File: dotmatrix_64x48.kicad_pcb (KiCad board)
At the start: 2 copper layers, 226 x 136 mm, 882 parts, among them J1 CONN_01X04, J2 CONN_01X05, P3 CONN_01X06, P6 CONN_01X03, Q1 Q_NPN_BCE RN5006, Q10 AO3401, Q11 AO3401, Q12 AO3401, Q13 AO3401, Q14 AO3401, Q15 AO3401, Q16 AO3401, Q17 AO3401, Q18 AO3401, Q19 AO3401, Q2 Q_NPN_BEC, Q20 AO3401, Q21 AO3401, Q22 AO3401, Q23 AO3401, Q24 AO3401, Q25 AO3401, Q26 AO3401, Q27 AO3401, Q28 AO3401, Q29 AO3401, Q3 NJL7302L-F3, Q30 Q_NPN_BEC, Q4 Q_NPN_BEC, Q5 AO3401, Q6 AO3401, Q7 AO3401, Q8 AO3401, Q9 AO3401, SW1 SW_PUSH_SMALL_H, SW2 SW_PUSH_SMALL_H, SW3 SW_PUSH_SMALL_H, SW4 SW_PUSH_SMALL_H, SW5 SW_PUSH_SMALL_H, SW6 SW_PUSH_SMALL_H, SW7 SW_PUSH_SMALL_H, SW8 SW_PUSH_SMALL_H, T1 COMMON_MODE_CHOKE, U1 WROOM-02, U10 LED1642GW, U11 74HCT595, U12 AE-BME280, U13 74HCT595, U14 NJM2845DL1-33, U15 74HCT595, U17 OSRB38C9AA, U18 BME280, U19 PIC32MX220F032B-I/ML, U2 74VHC541, U3 LED1642GW, U4 LED1642GW, U5 LED1642GW, U6 LED1642GW, U7 LED1642GW, U8 LED1642GW, U9 LED1642GW, Y1 8MHz

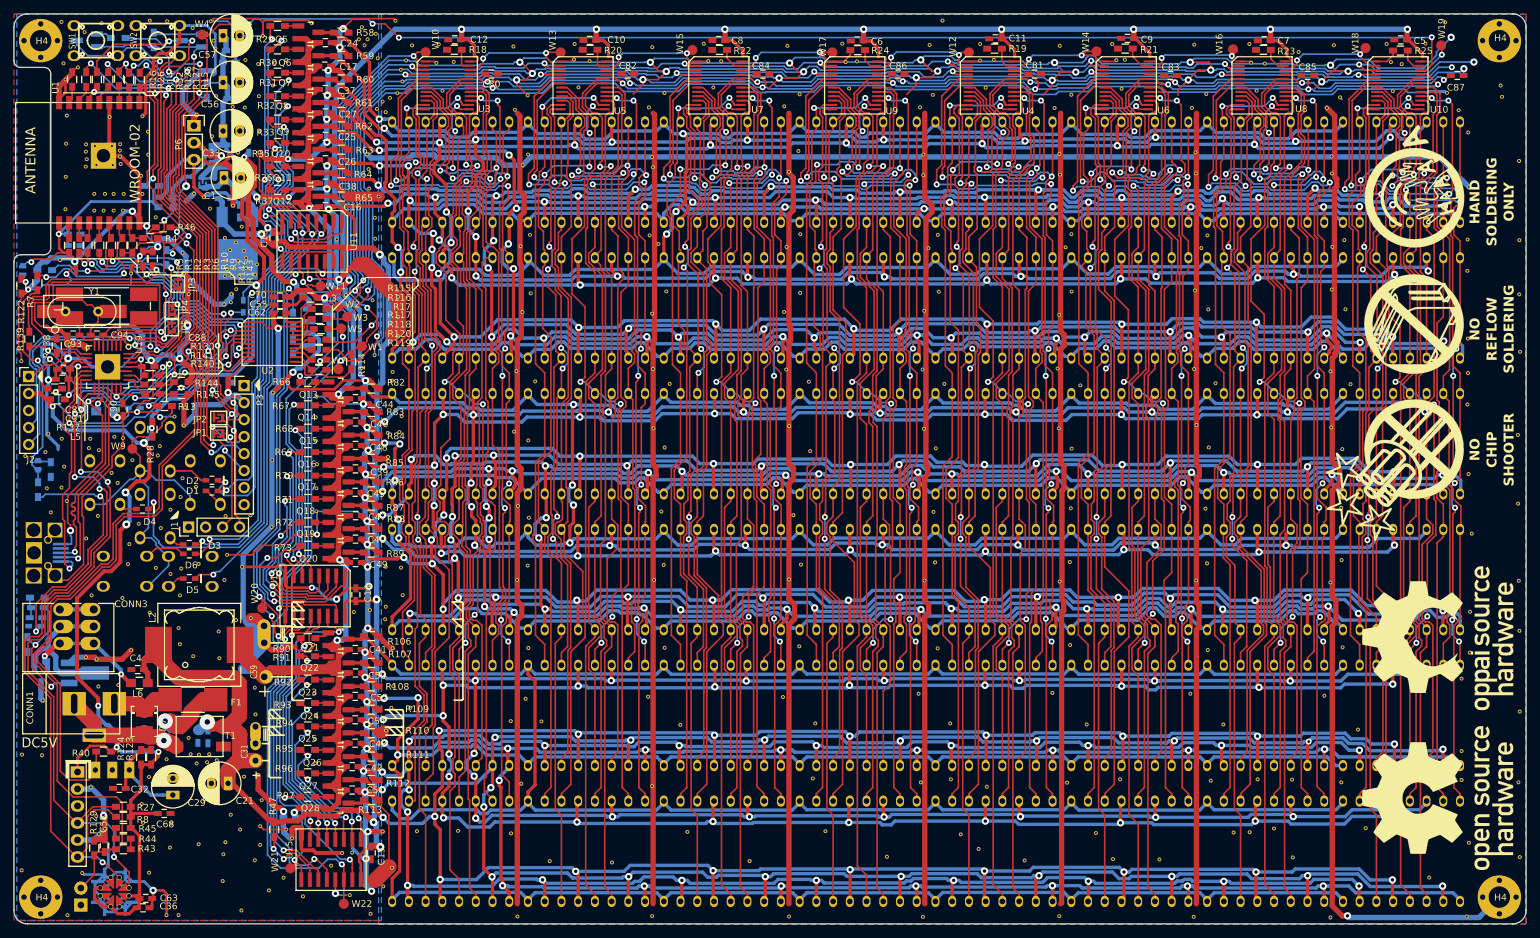
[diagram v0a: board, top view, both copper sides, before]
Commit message: DRC clear; This project likely to be abandoned due to 4MiB Flash version WROOM-02 shortage.
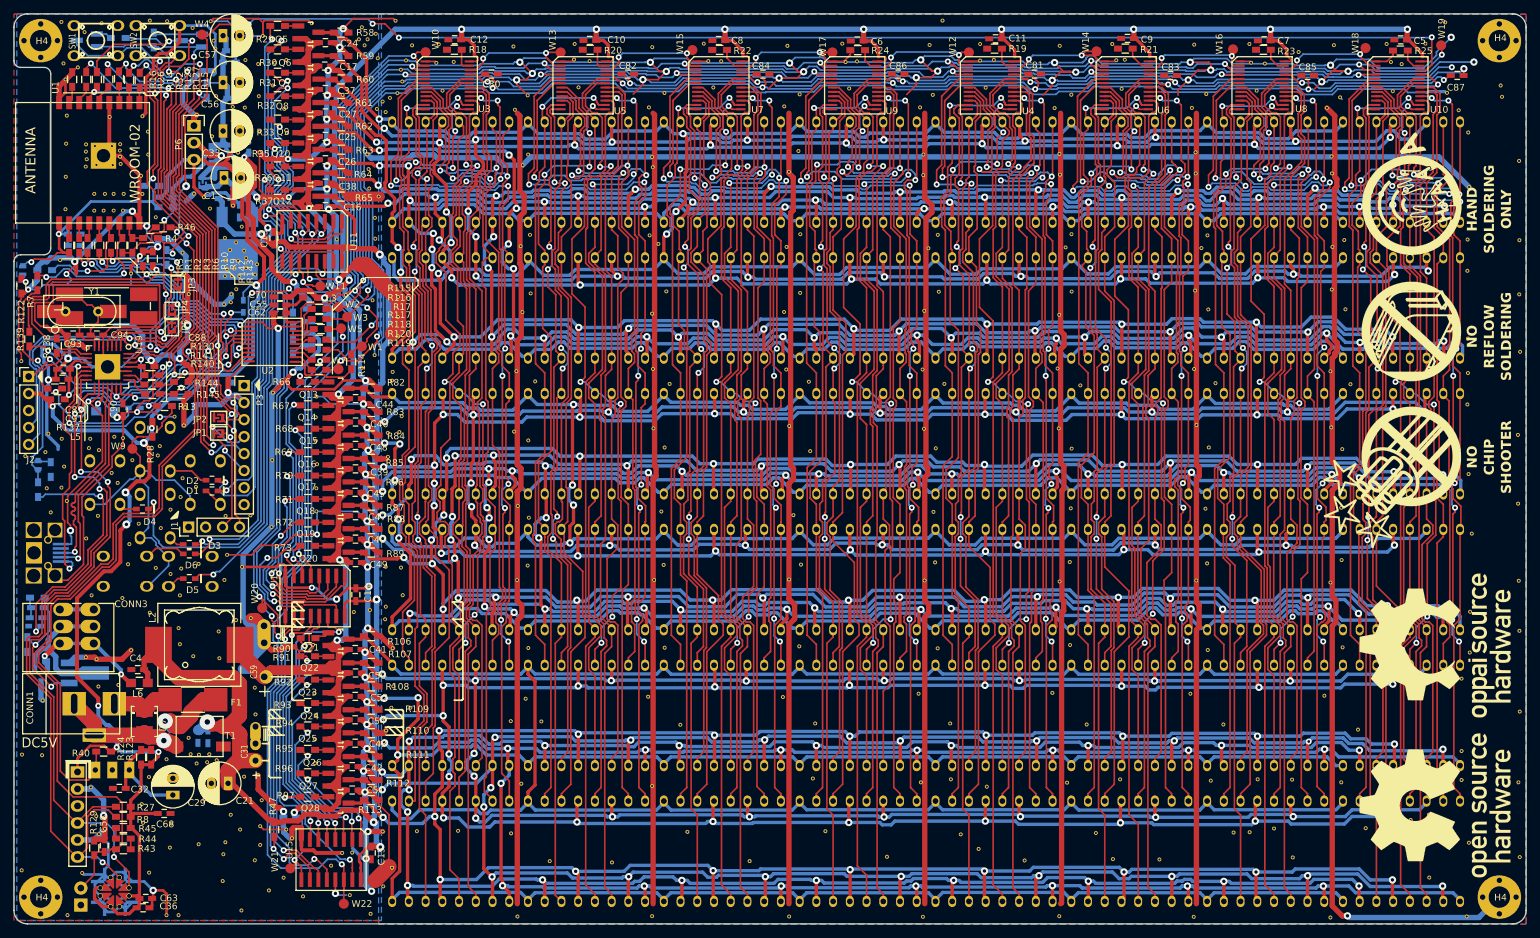
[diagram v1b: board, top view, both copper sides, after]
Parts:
- added REF**: stitch-via-0.6mm, components:stitch-via-0.6mm, F.Cu at (52.8, 29.8)
- added REF**: stitch-via-0.6mm, components:stitch-via-0.6mm, F.Cu at (52.4, 26.2)
- moved G*** 1.17 mm to (222.0, 85.3)
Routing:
- net GND: track 3088.4 -> 3084.8 mm
- net /row_driver/SEL4: track 100.5 -> 103.5 mm
- net /row_driver/SEL5: track 86.1 -> 85.6 mm

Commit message: This is the MazoClock hw 4.0 series; Uses ESP32 processor instead of ESP8266 used in prior MazoClock hw 3.0 series.
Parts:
- removed C33, C56, C57: 100u, components:C_Radial_D6.3_L11.2_P2.5_hand_soldering
- removed C34, C35, C69, C71: 1u, Capacitors_SMD:C_0603_HandSoldering
- removed C61: 0.1u, Capacitors_SMD:C_0603_HandSoldering
- removed D10, D8: Led_Small, components:LED1608_Handsoldering
- removed JP13: Jumper_NC_Small, components:SolderJumper
- removed L1: BLM21PG331SN 300R@100MHz, Capacitors_SMD:C_0805_HandSoldering
- removed L4, L7: BLM18RK102SN1 1k @ 100MHz, Resistors_SMD:R_0603_HandSoldering
- removed P3: CONN_01X06, Pin_Headers:Pin_Header_Straight_1x08_Pitch2.54mm
- removed P6: CONN_01X03, Pin_Headers:Pin_Header_Straight_1x03
- removed R121, R142, R143, R144, R145, R38, R39: 22k, Resistors_SMD:R_0603_HandSoldering
- removed R122: 4.7k, Resistors_SMD:R_0603_HandSoldering
- removed R126, R127, R46, R52: 120R, Resistors_SMD:R_0603_HandSoldering
- removed R48: 1k, Resistors_SMD:R_0603_HandSoldering
- removed R54, R55: 10k, Resistors_SMD:R_0603_HandSoldering
- removed the REF** at (48.5, 19.5)
- removed the REF** at (45.5, 48.9)
- removed the REF** at (18.9, 48.8)
- removed the REF** at (229.9, 89.7)
- removed the REF** at (38.9, 38.9)
- removed the REF** at (210.4, 93.6)
- removed the REF** at (229.4, 80.8)
- removed the REF** at (229.2, 70.4)
- removed the REF** at (229.3, 65.7)
- removed the REF** at (44.4, 55.1)
- removed the REF** at (211.8, 67.3)
- removed the REF** at (45.2, 53.1)
- removed the REF** at (46.4, 47.4)
- removed the REF** at (44.3, 47.3)
- removed the REF** at (46.0, 43.8)
- removed the REF** at (44.8, 40.6)
- removed the REF** at (229.3, 60.5)
- removed the REF** at (43.5, 45.5)
- removed the REF** at (45.2, 46.1)
- removed the REF** at (65.6, 54.8)
- removed the REF** at (65.1, 38.1)
- removed the REF** at (65.0, 35.2)
- removed the REF** at (64.8, 33.0)
- removed the REF** at (41.9, 16.0)
- removed the REF** at (47.1, 31.2)
- removed the REF** at (31.0, 36.2)
- removed the REF** at (32.0, 29.6)
- removed the REF** at (19.8, 36.4)
- removed the REF** at (19.8, 31.4)
- removed the REF** at (21.6, 20.0)
- removed the REF** at (46.5, 26.0)
- removed the REF** at (24.3, 131.9)
- removed the REF** at (13.2, 140.0)
- removed the REF** at (46.6, 18.9)
- removed the REF** at (66.0, 45.6)
- removed the REF** at (42.2, 24.3)
- removed the REF** at (50.6, 78.7)
- removed the REF** at (38.1, 120.2)
- removed the REF** at (45.2, 102.6)
- removed the REF** at (36.8, 106.2)
- removed the REF** at (44.7, 25.9)
- removed the REF** at (35.5, 133.0)
- removed the REF** at (38.8, 108.0)
- removed the REF** at (42.6, 104.3)
- removed the REF** at (32.3, 101.5)
- removed the REF** at (36.6, 103.8)
- removed the REF** at (35.3, 136.6)
- removed the REF** at (44.4, 131.7)
- removed the REF** at (46.4, 126.0)
- removed the REF** at (43.3, 137.6)
- removed the REF** at (45.8, 133.9)
- removed the REF** at (43.6, 135.8)
- removed the REF** at (39.6, 136.1)
- removed the REF** at (32.1, 33.0)
- removed the REF** at (38.1, 53.9)
- removed the REF** at (22.7, 34.8)
- removed the REF** at (22.9, 33.7)
- removed the REF** at (22.8, 32.6)
- removed the REF** at (22.8, 31.5)
- removed the REF** at (26.6, 31.8)
- removed the REF** at (24.1, 31.8)
- removed the REF** at (24.3, 34.6)
- removed the REF** at (26.8, 34.6)
- removed the REF** at (27.9, 34.4)
- removed the REF** at (27.9, 33.4)
- removed the REF** at (27.8, 32.4)
- removed the REF** at (27.9, 31.5)
- removed the REF** at (22.6, 14.7)
- removed the REF** at (43.6, 87.0)
- removed the REF** at (34.8, 123.4)
- removed the REF** at (32.2, 126.0)
- removed the REF** at (39.3, 124.0)
- removed the REF** at (40.9, 123.8)
- removed the REF** at (42.3, 123.5)
- removed the REF** at (39.6, 122.7)
- removed the REF** at (38.4, 122.7)
- removed the REF** at (41.2, 122.7)
- removed the REF** at (40.5, 129.4)
- removed the REF** at (42.7, 108.3)
- removed the REF** at (66.0, 42.5)
- removed the REF** at (45.5, 32.7)
- removed the REF** at (61.1, 24.1)
- removed the REF** at (66.4, 18.6)
- removed the REF** at (30.6, 88.2)
- removed the REF** at (46.1, 94.7)
- removed the REF** at (43.5, 96.6)
- removed the REF** at (34.0, 88.8)
- removed the REF** at (29.2, 91.2)
- removed the REF** at (47.4, 87.0)
- removed the REF** at (22.8, 108.2)
- removed the REF** at (44.6, 51.2)
- removed the REF** at (46.7, 50.0)
- removed the REF** at (45.0, 50.1)
- removed the REF** at (43.8, 50.1)
- removed the REF** at (37.6, 70.8)
- removed the REF** at (36.0, 72.2)
- removed the REF** at (33.8, 76.6)
- removed the REF** at (23.2, 76.9)
- removed the REF** at (19.9, 84.8)
- removed the REF** at (48.0, 51.0)
- removed the REF** at (17.5, 86.5)
- removed the REF** at (19.1, 82.8)
- removed the REF** at (16.9, 82.9)
- removed the REF** at (13.7, 78.1)
- removed the REF** at (17.1, 74.8)
- removed the REF** at (39.2, 82.7)
- removed the REF** at (29.5, 50.8)
- removed the REF** at (19.7, 21.8)
- removed the REF** at (19.4, 19.4)
- removed the REF** at (41.6, 30.3)
- removed the REF** at (44.7, 20.7)
- removed the REF** at (44.7, 28.0)
- removed the REF** at (41.4, 13.1)
- removed the REF** at (34.9, 13.1)
- removed the REF** at (32.3, 13.0)
- removed the REF** at (35.4, 86.1)
- removed the REF** at (36.9, 84.2)
- removed the REF** at (27.5, 82.1)
- removed the REF** at (26.6, 80.6)
- removed the REF** at (33.2, 42.4)
- removed the REF** at (31.2, 38.9)
- removed the REF** at (26.3, 27.4)
- removed the REF** at (31.2, 27.3)
- removed the REF** at (19.9, 27.2)
- removed the REF** at (19.7, 41.2)
- removed the REF** at (19.1, 13.2)
- removed the REF** at (25.1, 13.4)
- removed the REF** at (38.7, 14.1)
- removed the REF** at (41.9, 20.5)
- removed the REF** at (29.1, 94.2)
- removed the REF** at (36.8, 98.9)
- removed the REF** at (43.9, 92.8)
- removed the REF** at (37.0, 94.9)
- removed the REF** at (35.4, 95.7)
- removed the REF** at (33.2, 94.8)
- removed the REF** at (39.6, 94.2)
- removed the REF** at (37.2, 81.4)
- removed the REF** at (33.5, 78.0)
- removed the REF** at (29.7, 78.7)
- removed the REF** at (28.4, 38.9)
- removed the REF** at (26.9, 38.9)
- removed the REF** at (25.6, 38.9)
- removed the REF** at (24.0, 38.9)
- removed the REF** at (28.3, 41.4)
- removed the REF** at (26.9, 41.4)
- removed the REF** at (25.4, 41.4)
- removed the REF** at (24.0, 41.4)
- removed the REF** at (37.2, 47.7)
- removed the REF** at (48.7, 29.6)
- removed the REF** at (48.7, 32.7)
- removed the REF** at (41.3, 41.1)
- removed the REF** at (40.4, 39.4)
- removed the REF** at (50.7, 68.6)
- removed the REF** at (37.4, 50.8)
- removed the REF** at (44.5, 53.9)
- removed the REF** at (43.5, 51.2)
- removed the REF** at (45.7, 51.2)
- removed the REF** at (46.7, 48.5)
- removed the REF** at (43.6, 48.9)
- removed the REF** at (43.4, 55.4)
- removed the REF** at (19.1, 75.5)
- removed the REF** at (28.3, 75.4)
- removed the REF** at (27.0, 75.2)
- removed the REF** at (23.4, 75.5)
- removed the REF** at (13.1, 63.9)
- removed the REF** at (37.4, 73.5)
- removed the REF** at (24.7, 77.2)
- removed the REF** at (19.5, 79.7)
- removed the REF** at (16.7, 77.5)
- removed the REF** at (22.8, 90.4)
- removed the REF** at (24.6, 87.0)
- removed the REF** at (28.2, 99.3)
- removed the REF** at (29.5, 107.1)
- removed the REF** at (24.7, 134.6)
- removed the REF** at (48.3, 49.4)
- removed the REF** at (46.0, 146.0)
- removed the REF** at (50.1, 143.0)
- removed the REF** at (43.2, 141.6)
- removed the REF** at (25.6, 133.8)
- removed the REF** at (31.3, 132.9)
- removed the REF** at (31.1, 130.1)
- removed the REF** at (23.5, 127.6)
- removed the REF** at (39.3, 27.1) (x2)
- removed the REF** at (42.1, 17.2)
- removed the REF** at (48.6, 24.3)
- removed SW1, SW2: SW_PUSH_SMALL_H, components:TACT-SW-4P
- removed W4, W5, W9: TEST_1P, Measurement_Points:Measurement_Point_Round-SMD-Pad_Small
- added C28: 1u, Capacitors_SMD:C_0603_HandSoldering, F.Cu at (28.9, 89.8)
- added C30: 1u, Capacitors_SMD:C_0603_HandSoldering, F.Cu at (30.3, 72.2)
- added J10: Conn_01x07_Female, Pin_Headers:Pin_Header_Straight_1x07_Pitch2.54mm, F.Cu at (254.4, 73.2)
- added J11: Conn_01x04_Female, Pin_Headers:Pin_Header_Straight_1x04_Pitch2.54mm, B.Cu at (50.2, 100.3)
- added J3: Conn_01x19_Female, Pin_Headers:Pin_Header_Straight_1x19_Pitch2.54mm, B.Cu at (26.2, 65.5)
- added J4: Conn_01x14_Female, Pin_Headers:Pin_Header_Straight_1x14_Pitch2.54mm, B.Cu at (14.5, 72.0)
- added J5: Conn_01x10_Female, Pin_Headers:Pin_Header_Straight_1x10_Pitch2.54mm, B.Cu at (58.4, 71.1)
- added J6: Conn_01x10_Female, Pin_Headers:Pin_Header_Straight_1x10_Pitch2.54mm, B.Cu at (66.0, 71.1)
- added J7: Conn_01x03_Female, Pin_Headers:Pin_Header_Straight_1x03_Pitch2.54mm, B.Cu at (22.9, 71.1)
- added J8: Conn_01x08_Female, Pin_Headers:Pin_Header_Straight_1x08_Pitch2.54mm, F.Cu at (17.4, 21.4)
- added J9: Conn_01x07_Female, Pin_Headers:Pin_Header_Straight_1x07_Pitch2.54mm, F.Cu at (13.9, 100.5)
- added JP10: Jumper_NC_Small, components:SolderJumper, F.Cu at (61.0, 89.0)
- added JP11: Jumper_NC_Small, components:SolderJumper, F.Cu at (61.0, 91.5)
- added JP12: Jumper_NC_Small, components:SolderJumper, F.Cu at (61.0, 94.0)
- added JP6: Jumper_NC_Small, components:SolderJumper, F.Cu at (61.0, 76.0)
- added JP7: Jumper_NC_Small, components:SolderJumper, F.Cu at (61.0, 81.5)
- added JP8: Jumper_NC_Small, components:SolderJumper, F.Cu at (61.0, 84.0)
- added JP9: Jumper_NC_Small, components:SolderJumper, F.Cu at (61.0, 86.5)
- added REF**: stitch-via-0.6mm, components:stitch-via-0.6mm, F.Cu at (42.4, 137.3)
- added REF**: stitch-via-0.6mm, components:stitch-via-0.6mm, F.Cu at (42.7, 115.7)
- added REF**: stitch-via-0.6mm, components:stitch-via-0.6mm, F.Cu at (60.4, 109.4)
- added REF**: stitch-via-0.6mm, components:stitch-via-0.6mm, F.Cu at (57.1, 112.1)
- added REF**: stitch-via-0.6mm, components:stitch-via-0.6mm, F.Cu at (47.8, 116.8)
- added REF**: stitch-via-0.6mm, components:stitch-via-0.6mm, B.Cu at (24.9, 56.6)
- added REF**: stitch-via-0.6mm, components:stitch-via-0.6mm, B.Cu at (22.1, 51.9)
- added REF**: stitch-via-0.6mm, components:stitch-via-0.6mm, F.Cu at (68.7, 130.9)
- added REF**: stitch-via-0.6mm, components:stitch-via-0.6mm, F.Cu at (58.2, 130.6)
- added REF**: stitch-via-0.6mm, components:stitch-via-0.6mm, F.Cu at (63.5, 130.5)
- added REF**: stitch-via-0.6mm, components:stitch-via-0.6mm, B.Cu at (23.6, 40.0)
- added REF**: stitch-via-0.6mm, components:stitch-via-0.6mm, B.Cu at (17.3, 41.3)
- added REF**: stitch-via-0.6mm, components:stitch-via-0.6mm, F.Cu at (68.5, 17.9)
- added REF**: stitch-via-0.6mm, components:stitch-via-0.6mm, B.Cu at (21.7, 39.6)
- added REF**: stitch-via-0.6mm, components:stitch-via-0.6mm, F.Cu at (86.7, 45.1)
- added REF**: stitch-via-0.6mm, components:stitch-via-0.6mm, F.Cu at (86.6, 42.1)
- added REF**: stitch-via-0.6mm, components:stitch-via-0.6mm, B.Cu at (18.7, 19.1)
- added REF**: stitch-via-0.6mm, components:stitch-via-0.6mm, B.Cu at (21.7, 13.2)
- added REF**: stitch-via-0.6mm, components:stitch-via-0.6mm, F.Cu at (47.4, 74.9)
- added REF**: stitch-via-0.6mm, components:stitch-via-0.6mm, F.Cu at (52.6, 119.4)
- added REF**: stitch-via-0.6mm, components:stitch-via-0.6mm, F.Cu at (52.7, 112.2)
- added REF**: stitch-via-0.6mm, components:stitch-via-0.6mm, F.Cu at (66.1, 121.4)
- added REF**: stitch-via-0.6mm, components:stitch-via-0.6mm, F.Cu at (66.1, 119.1)
- added REF**: stitch-via-0.6mm, components:stitch-via-0.6mm, F.Cu at (47.9, 81.6)
- added REF**: stitch-via-0.6mm, components:stitch-via-0.6mm, F.Cu at (67.3, 106.4)
- added REF**: stitch-via-0.6mm, components:stitch-via-0.6mm, F.Cu at (69.4, 108.3)
- added REF**: stitch-via-0.6mm, components:stitch-via-0.6mm, F.Cu at (66.2, 106.4)
- added REF**: stitch-via-0.6mm, components:stitch-via-0.6mm, F.Cu at (64.4, 108.2)
- added REF**: stitch-via-0.6mm, components:stitch-via-0.6mm, F.Cu at (66.5, 95.8)
- added REF**: stitch-via-0.6mm, components:stitch-via-0.6mm, F.Cu at (56.6, 94.2)
- added REF**: stitch-via-0.6mm, components:stitch-via-0.6mm, F.Cu at (45.2, 131.9)
- added REF**: stitch-via-0.6mm, components:stitch-via-0.6mm, F.Cu at (43.1, 132.9)
- added REF**: stitch-via-0.6mm, components:stitch-via-0.6mm, F.Cu at (56.6, 125.6)
- added REF**: stitch-via-0.6mm, components:stitch-via-0.6mm, F.Cu at (63.7, 128.6)
- added REF**: stitch-via-0.6mm, components:stitch-via-0.6mm, F.Cu at (17.7, 108.1)
- added REF**: stitch-via-0.6mm, components:stitch-via-0.6mm, F.Cu at (67.6, 143.8)
- added REF**: stitch-via-0.6mm, components:stitch-via-0.6mm, F.Cu at (67.4, 146.8)
- added REF**: stitch-via-0.6mm, components:stitch-via-0.6mm, F.Cu at (72.7, 146.8)
- added REF**: stitch-via-0.6mm, components:stitch-via-0.6mm, F.Cu at (61.1, 137.7)
- added REF**: stitch-via-0.6mm, components:stitch-via-0.6mm, F.Cu at (62.5, 142.4)
- added REF**: stitch-via-0.6mm, components:stitch-via-0.6mm, F.Cu at (53.7, 146.8)
- added REF**: stitch-via-0.6mm, components:stitch-via-0.6mm, F.Cu at (35.5, 140.9)
- added REF**: stitch-via-0.6mm, components:stitch-via-0.6mm, F.Cu at (33.1, 133.6)
- added REF**: stitch-via-0.6mm, components:stitch-via-0.6mm, F.Cu at (28.5, 122.6)
- added REF**: stitch-via-0.6mm, components:stitch-via-0.6mm, F.Cu at (36.0, 122.3)
- added REF**: stitch-via-0.6mm, components:stitch-via-0.6mm, F.Cu at (26.4, 115.7)
- added REF**: stitch-via-0.6mm, components:stitch-via-0.6mm, F.Cu at (33.0, 130.1)
- added REF**: stitch-via-0.6mm, components:stitch-via-0.6mm, F.Cu at (55.1, 131.7)
- added REF**: stitch-via-0.6mm, components:stitch-via-0.6mm, F.Cu at (44.8, 132.9)
- added REF**: stitch-via-0.6mm, components:stitch-via-0.6mm, F.Cu at (44.9, 130.8)
- added REF**: stitch-via-0.6mm, components:stitch-via-0.6mm, F.Cu at (36.8, 137.1)
- added REF**: stitch-via-0.6mm, components:stitch-via-0.6mm, F.Cu at (52.7, 135.5)
- added REF**: stitch-via-0.6mm, components:stitch-via-0.6mm, F.Cu at (50.1, 135.6)
- added REF**: stitch-via-0.6mm, components:stitch-via-0.6mm, F.Cu at (45.0, 135.9)
- added REF**: stitch-via-0.6mm, components:stitch-via-0.6mm, F.Cu at (47.5, 132.5)
- added REF**: stitch-via-0.6mm, components:stitch-via-0.6mm, F.Cu at (27.8, 90.4)
- added REF**: stitch-via-0.6mm, components:stitch-via-0.6mm, F.Cu at (30.7, 115.8)
- added REF**: stitch-via-0.6mm, components:stitch-via-0.6mm, F.Cu at (32.5, 89.8)
- added REF**: stitch-via-0.6mm, components:stitch-via-0.6mm, F.Cu at (65.2, 113.1)
- added REF**: stitch-via-0.6mm, components:stitch-via-0.6mm, F.Cu at (29.2, 68.9)
- added REF**: stitch-via-0.6mm, components:stitch-via-0.6mm, F.Cu at (29.3, 104.6)
- added REF**: stitch-via-0.6mm, components:stitch-via-0.6mm, F.Cu at (27.6, 118.4)
- added REF**: stitch-via-0.6mm, components:stitch-via-0.6mm, F.Cu at (33.5, 119.1)
- added REF**: stitch-via-0.6mm, components:stitch-via-0.6mm, F.Cu at (47.4, 126.0)
- added REF**: stitch-via-0.6mm, components:stitch-via-0.6mm, F.Cu at (44.1, 126.0)
- added REF**: stitch-via-0.6mm, components:stitch-via-0.6mm, F.Cu at (29.3, 75.1)
- added REF**: stitch-via-0.6mm, components:stitch-via-0.6mm, F.Cu at (35.5, 71.0)
- added REF**: stitch-via-0.6mm, components:stitch-via-0.6mm, B.Cu at (67.4, 99.5)
- added REF**: stitch-via-0.6mm, components:stitch-via-0.6mm, F.Cu at (54.3, 75.7)
- added REF**: stitch-via-0.6mm, components:stitch-via-0.6mm, F.Cu at (50.5, 89.3)
- added REF**: stitch-via-0.6mm, components:stitch-via-0.6mm, F.Cu at (47.2, 88.7)
- added REF**: stitch-via-0.6mm, components:stitch-via-0.6mm, F.Cu at (35.4, 83.3)
- added REF**: stitch-via-0.6mm, components:stitch-via-0.6mm, F.Cu at (27.7, 78.3)
- added REF**: stitch-via-0.6mm, components:stitch-via-0.6mm, F.Cu at (33.9, 73.1)
- added REF**: stitch-via-0.6mm, components:stitch-via-0.6mm, F.Cu at (52.1, 71.2)
- added REF**: stitch-via-0.6mm, components:stitch-via-0.6mm, B.Cu at (41.8, 64.4)
- added REF**: stitch-via-0.6mm, components:stitch-via-0.6mm, F.Cu at (22.9, 69.0)
- added REF**: stitch-via-0.6mm, components:stitch-via-0.6mm, B.Cu at (63.5, 41.3)
- added REF**: stitch-via-0.6mm, components:stitch-via-0.6mm, B.Cu at (71.3, 66.3)
- added REF**: stitch-via-0.6mm, components:stitch-via-0.6mm, B.Cu at (64.1, 46.3)
- added REF**: stitch-via-0.6mm, components:stitch-via-0.6mm, B.Cu at (71.2, 60.4)
- added REF**: stitch-via-0.6mm, components:stitch-via-0.6mm, B.Cu at (59.9, 64.1)
- added REF**: stitch-via-0.6mm, components:stitch-via-0.6mm, B.Cu at (50.8, 58.0)
- added REF**: stitch-via-0.6mm, components:stitch-via-0.6mm, B.Cu at (65.1, 17.7)
- added REF**: stitch-via-0.6mm, components:stitch-via-0.6mm, B.Cu at (50.7, 23.4)
- added REF**: stitch-via-0.6mm, components:stitch-via-0.6mm, B.Cu at (50.5, 31.5)
- added REF**: stitch-via-0.6mm, components:stitch-via-0.6mm, B.Cu at (37.3, 22.9)
- added REF**: stitch-via-0.6mm, components:stitch-via-0.6mm, B.Cu at (38.2, 34.8)
- added REF**: stitch-via-0.6mm, components:stitch-via-0.6mm, B.Cu at (37.6, 19.0)
- added REF** (x2): stitch-via-0.6mm, components:stitch-via-0.6mm, F.Cu at (57.3, 102.3)
- added REF**: stitch-via-0.6mm, components:stitch-via-0.6mm, B.Cu at (41.1, 31.4)
- added REF**: stitch-via-0.6mm, components:stitch-via-0.6mm, B.Cu at (43.7, 44.4)
- added REF**: stitch-via-0.6mm, components:stitch-via-0.6mm, B.Cu at (43.7, 47.6)
- added REF**: stitch-via-0.6mm, components:stitch-via-0.6mm, B.Cu at (43.7, 50.9)
- added REF**: stitch-via-0.6mm, components:stitch-via-0.6mm, B.Cu at (41.0, 51.8)
- added REF**: stitch-via-0.6mm, components:stitch-via-0.6mm, B.Cu at (38.5, 51.9)
- added REF**: stitch-via-0.6mm, components:stitch-via-0.6mm, B.Cu at (34.5, 57.2)
- added REF**: stitch-via-0.6mm, components:stitch-via-0.6mm, B.Cu at (36.3, 56.9)
- added REF**: stitch-via-0.6mm, components:stitch-via-0.6mm, B.Cu at (38.5, 56.2)
- added REF**: stitch-via-0.6mm, components:stitch-via-0.6mm, B.Cu at (37.3, 58.8)
- added REF**: stitch-via-0.6mm, components:stitch-via-0.6mm, B.Cu at (65.2, 133.9)
- added REF**: stitch-via-0.6mm, components:stitch-via-0.6mm, B.Cu at (35.3, 59.8)
- added REF**: stitch-via-0.6mm, components:stitch-via-0.6mm, B.Cu at (39.8, 58.5)
- added REF**: stitch-via-0.6mm, components:stitch-via-0.6mm, B.Cu at (36.2, 54.6)
- added REF**: stitch-via-0.6mm, components:stitch-via-0.6mm, B.Cu at (34.2, 54.9)
- added REF**: stitch-via-0.6mm, components:stitch-via-0.6mm, B.Cu at (38.4, 54.2)
- added REF**: stitch-via-0.6mm, components:stitch-via-0.6mm, B.Cu at (35.8, 61.1)
- added REF**: stitch-via-0.6mm, components:stitch-via-0.6mm, B.Cu at (43.5, 57.4)
- added REF**: stitch-via-0.6mm, components:stitch-via-0.6mm, B.Cu at (43.6, 54.5)
- added REF**: stitch-via-0.6mm, components:stitch-via-0.6mm, B.Cu at (46.4, 57.1)
- added REF**: stitch-via-0.6mm, components:stitch-via-0.6mm, B.Cu at (49.4, 62.0)
- added REF**: stitch-via-0.6mm, components:stitch-via-0.6mm, F.Cu at (42.8, 101.0)
- added REF**: stitch-via-0.6mm, components:stitch-via-0.6mm, B.Cu at (28.7, 130.0)
- added REF**: stitch-via-0.6mm, components:stitch-via-0.6mm, B.Cu at (46.4, 54.1)
- added REF**: stitch-via-0.6mm, components:stitch-via-0.6mm, B.Cu at (50.4, 46.1)
- added REF**: stitch-via-0.6mm, components:stitch-via-0.6mm, B.Cu at (34.4, 46.8)
- added REF**: stitch-via-0.6mm, components:stitch-via-0.6mm, B.Cu at (35.1, 51.8)
- added REF**: stitch-via-0.6mm, components:stitch-via-0.6mm, B.Cu at (41.9, 29.5)
- added REF**: stitch-via-0.6mm, components:stitch-via-0.6mm, B.Cu at (46.7, 29.7)
- added REF**: stitch-via-0.6mm, components:stitch-via-0.6mm, B.Cu at (46.7, 24.8)
- added REF**: stitch-via-0.6mm, components:stitch-via-0.6mm, B.Cu at (42.1, 24.9)
- added REF**: stitch-via-0.6mm, components:stitch-via-0.6mm, B.Cu at (15.7, 118.4)
- added REF**: stitch-via-0.6mm, components:stitch-via-0.6mm, B.Cu at (20.4, 116.8)
- added REF**: stitch-via-0.6mm, components:stitch-via-0.6mm, B.Cu at (48.1, 86.6)
- added REF**: stitch-via-0.6mm, components:stitch-via-0.6mm, B.Cu at (30.8, 86.7)
- added REF**: stitch-via-0.6mm, components:stitch-via-0.6mm, B.Cu at (38.8, 86.8)
- added REF**: stitch-via-0.6mm, components:stitch-via-0.6mm, B.Cu at (22.7, 58.9)
- added REF**: stitch-via-0.6mm, components:stitch-via-0.6mm, B.Cu at (67.8, 44.0)
- added REF**: stitch-via-0.6mm, components:stitch-via-0.6mm, B.Cu at (67.7, 37.7)
- added REF**: stitch-via-0.6mm, components:stitch-via-0.6mm, B.Cu at (46.4, 40.9)
- added REF**: stitch-via-0.6mm, components:stitch-via-0.6mm, F.Cu at (42.8, 89.5)
- added REF**: stitch-via-0.6mm, components:stitch-via-0.6mm, B.Cu at (43.6, 40.9)
- added REF**: stitch-via-0.6mm, components:stitch-via-0.6mm, B.Cu at (60.3, 17.6)
- added REF**: stitch-via-0.6mm, components:stitch-via-0.6mm, B.Cu at (61.7, 13.9)
- added REF**: stitch-via-0.6mm, components:stitch-via-0.6mm, B.Cu at (26.5, 14.1)
- added REF**: stitch-via-0.6mm, components:stitch-via-0.6mm, B.Cu at (50.5, 19.1)
- added REF**: stitch-via-0.6mm, components:stitch-via-0.6mm, B.Cu at (43.8, 19.2)
- added REF**: stitch-via-0.6mm, components:stitch-via-0.6mm, B.Cu at (50.7, 27.5)
- added REF**: stitch-via-0.6mm, components:stitch-via-0.6mm, F.Cu at (54.4, 73.1)
- added REF**: stitch-via-0.6mm, components:stitch-via-0.6mm, F.Cu at (38.2, 81.5)
- added REF**: stitch-via-0.6mm, components:stitch-via-0.6mm, F.Cu at (32.0, 81.8)
- added REF**: stitch-via-0.6mm, components:stitch-via-0.6mm, F.Cu at (42.0, 93.3)
- added REF**: stitch-via-0.6mm, components:stitch-via-0.6mm, F.Cu at (62.9, 68.4)
- added REF**: stitch-via-0.6mm, components:stitch-via-0.6mm, F.Cu at (71.5, 77.4)
- added REF**: stitch-via-0.6mm, components:stitch-via-0.6mm, F.Cu at (68.3, 91.2)
- added REF**: stitch-via-0.6mm, components:stitch-via-0.6mm, F.Cu at (27.4, 101.4)
- added REF**: stitch-via-0.6mm, components:stitch-via-0.6mm, F.Cu at (27.8, 103.2)
- added REF**: stitch-via-0.6mm, components:stitch-via-0.6mm, F.Cu at (251.2, 63.4)
- added REF**: stitch-via-0.6mm, components:stitch-via-0.6mm, F.Cu at (249.3, 57.2)
- added REF**: stitch-via-0.6mm, components:stitch-via-0.6mm, F.Cu at (249.3, 93.6)
- added REF**: stitch-via-0.6mm, components:stitch-via-0.6mm, F.Cu at (252.3, 87.4)
- added REF**: stitch-via-0.6mm, components:stitch-via-0.6mm, F.Cu at (250.3, 84.5)
- added REF**: stitch-via-0.6mm, components:stitch-via-0.6mm, F.Cu at (47.1, 96.5)
- added REF**: stitch-via-0.6mm, components:stitch-via-0.6mm, F.Cu at (252.2, 77.7)
- added REF**: stitch-via-0.6mm, components:stitch-via-0.6mm, B.Cu at (46.7, 34.9)
- added REF**: stitch-via-0.6mm, components:stitch-via-0.6mm, B.Cu at (41.5, 34.7)
- added REF**: stitch-via-0.6mm, components:stitch-via-0.6mm, F.Cu at (42.0, 97.3)
- added REF**: stitch-via-0.6mm, components:stitch-via-0.6mm, F.Cu at (61.4, 73.3)
- added REF**: stitch-via-0.6mm, components:stitch-via-0.6mm, F.Cu at (61.6, 78.7)
- added REF**: stitch-via-0.6mm, components:stitch-via-0.6mm, F.Cu at (85.4, 33.3)
- added REF**: stitch-via-0.6mm, components:stitch-via-0.6mm, F.Cu at (85.4, 35.8)
- added REF**: stitch-via-0.6mm, components:stitch-via-0.6mm, F.Cu at (87.8, 92.6)
- added REF**: stitch-via-0.6mm, components:stitch-via-0.6mm, F.Cu at (28.7, 23.4)
- added REF**: stitch-via-0.6mm, components:stitch-via-0.6mm, F.Cu at (47.3, 100.9)
- added REF**: stitch-via-0.6mm, components:stitch-via-0.6mm, F.Cu at (28.6, 26.2)
- added REF**: stitch-via-0.6mm, components:stitch-via-0.6mm, F.Cu at (15.4, 25.6)
- added REF**: stitch-via-0.6mm, components:stitch-via-0.6mm, F.Cu at (13.1, 27.9)
- added REF**: stitch-via-0.6mm, components:stitch-via-0.6mm, F.Cu at (20.6, 41.2)
- added REF**: stitch-via-0.6mm, components:stitch-via-0.6mm, F.Cu at (23.5, 42.8)
- added REF**: stitch-via-0.6mm, components:stitch-via-0.6mm, F.Cu at (34.3, 44.1)
- added REF**: stitch-via-0.6mm, components:stitch-via-0.6mm, F.Cu at (40.1, 47.6)
- added REF**: stitch-via-0.6mm, components:stitch-via-0.6mm, F.Cu at (40.1, 44.7)
- added REF**: stitch-via-0.6mm, components:stitch-via-0.6mm, F.Cu at (47.1, 47.4)
- added REF**: stitch-via-0.6mm, components:stitch-via-0.6mm, F.Cu at (47.1, 44.9)
- added REF**: stitch-via-0.6mm, components:stitch-via-0.6mm, F.Cu at (52.1, 93.0)
- added REF**: stitch-via-0.6mm, components:stitch-via-0.6mm, F.Cu at (49.5, 71.1)
- added REF**: stitch-via-0.6mm, components:stitch-via-0.6mm, F.Cu at (39.4, 70.9)
- added REF**: stitch-via-0.6mm, components:stitch-via-0.6mm, F.Cu at (43.4, 70.9)
- added REF**: stitch-via-0.6mm, components:stitch-via-0.6mm, F.Cu at (46.2, 71.0)
- added REF**: stitch-via-0.6mm, components:stitch-via-0.6mm, F.Cu at (50.7, 68.0)
- added REF**: stitch-via-0.6mm, components:stitch-via-0.6mm, F.Cu at (39.5, 68.2)
- added REF**: stitch-via-0.6mm, components:stitch-via-0.6mm, F.Cu at (35.0, 68.1)
- added REF**: stitch-via-0.6mm, components:stitch-via-0.6mm, F.Cu at (25.5, 80.4)
- added REF**: stitch-via-0.6mm, components:stitch-via-0.6mm, F.Cu at (77.4, 126.7)
- added REF**: stitch-via-0.6mm, components:stitch-via-0.6mm, F.Cu at (74.1, 116.3)
- added REF**: stitch-via-0.6mm, components:stitch-via-0.6mm, F.Cu at (51.4, 78.8)
- added REF**: stitch-via-0.6mm, components:stitch-via-0.6mm, B.Cu at (59.5, 68.0)
- added REF**: stitch-via-0.6mm, components:stitch-via-0.6mm, B.Cu at (49.6, 57.1)
- added REF**: stitch-via-0.6mm, components:stitch-via-0.6mm, B.Cu at (41.8, 58.6)
- added REF**: stitch-via-0.6mm, components:stitch-via-0.6mm, B.Cu at (46.4, 60.0)
- added REF**: stitch-via-0.6mm, components:stitch-via-0.6mm, B.Cu at (53.9, 64.0)
- added REF**: stitch-via-0.6mm, components:stitch-via-0.6mm, F.Cu at (27.7, 87.0)
- added REF**: stitch-via-0.6mm, components:stitch-via-0.6mm, F.Cu at (46.4, 68.0)
- added REF**: stitch-via-0.6mm, components:stitch-via-0.6mm, F.Cu at (43.3, 67.8)
- added REF**: stitch-via-0.6mm, components:stitch-via-0.6mm, F.Cu at (19.1, 108.1)
- added REF**: stitch-via-0.6mm, components:stitch-via-0.6mm, F.Cu at (16.3, 105.1)
- added REF**: stitch-via-0.6mm, components:stitch-via-0.6mm, F.Cu at (40.8, 119.4)
- added REF**: stitch-via-0.6mm, components:stitch-via-0.6mm, F.Cu at (20.2, 102.0)
- added REF**: stitch-via-0.6mm, components:stitch-via-0.6mm, F.Cu at (16.6, 102.6)
- added REF**: stitch-via-0.6mm, components:stitch-via-0.6mm, F.Cu at (20.1, 98.4)
- added REF**: stitch-via-0.6mm, components:stitch-via-0.6mm, F.Cu at (52.9, 126.1)
- added REF**: stitch-via-0.6mm, components:stitch-via-0.6mm, F.Cu at (47.6, 121.1)
- added REF**: stitch-via-0.6mm, components:stitch-via-0.6mm, F.Cu at (58.9, 108.1)
- added REF**: stitch-via-0.6mm, components:stitch-via-0.6mm, F.Cu at (54.3, 110.3)
- added REF**: stitch-via-0.6mm, components:stitch-via-0.6mm, F.Cu at (60.2, 99.8)
- added REF**: stitch-via-0.6mm, components:stitch-via-0.6mm, F.Cu at (47.1, 108.6)
- added U16: ESP32-WROOM, components:ESP32-WROOM-AND-SIDE-PINS, B.Cu at (44.1, 24.8)
- C1, C21, C68, J2, R123, R124, R40, R45: moved to B.Cu
- C19, C22, C23: value 1u -> 100u; footprint Capacitors_SMD:C_0603_HandSoldering -> components:C_Radial_D6.3_L11.2_P2.5_hand_soldering
- D11, D13, SW3, SW4, SW5, SW6, SW7, SW8: moved to F.Cu
- J1: value CONN_01X04 -> Conn_01x19_Female; footprint Pin_Headers:Pin_Header_Straight_1x04_Pitch2.54mm -> Pin_Headers:Pin_Header_Straight_1x19_Pitch2.54mm; moved to B.Cu
- R1, R15, R26: value 120R -> 22k
- R10, R9: value 22k -> 4.7k
- R14: value 120R -> 10k; moved to B.Cu
- R16: value 10k -> 22k
- R17: value 10R -> 22k
- R27, R8: value 4.7k -> 22k
- R34: value 10k -> 22k; moved to F.Cu
- R5: value 10k -> 120R
- R7: value 120R -> 10k
- U1: value WROOM-02 -> ESP32-DEVKIT-C; footprint components:WROOM-02 -> components:ESP32-DEVKIT-C; moved to B.Cu
- U14: footprint TO_SOT_Packages_SMD:TO-252-2Lead -> TO_SOT_Packages_SMD:TO-252-2
- moved SW7 211.6 mm to (250.0, 96.0)
- moved SW4 210.0 mm to (242.0, 56.0), turned to 270 degrees
- moved SW5 209.1 mm to (242.0, 79.0), turned to 270 degrees
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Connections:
- C1 pad 1: Net-(C1-Pad1) -> VCC
- C18 pad 1: ESPVDD -> VCC
- C21 pad 1: VCC -> ESPVDD
- C22 pad 1: VCC -> ESPVDD
- C23 pad 1: Net-(C1-Pad1) -> ESPVDD
- D11 pad 2: P_ROW_DAT -> P_SER_DAT
- D13 pad 1: P_ROW_DAT -> P_SER_DAT
- J1 pad 1: Net-(J1-Pad1) -> ESPVDD
- J1 pad 2: GND -> E_EN
- J1 pad 3: P_RX -> Net-(J1-Pad3)
- J1 pad 4: P_TX -> Net-(J1-Pad4)
- JP1 pad 1: P_RX -> P_TX
- JP1 pad 2: E_TXD -> E_RX
- JP2 pad 1: P_TX -> P_RX
- JP2 pad 2: E_RXD -> E_TX
- JP3 pad 1: P_MCLR -> P_ESP_GPIO0
- JP3 pad 2: E_MCLR -> E_GPIO0
- JP4 pad 1: P_PGED -> P_ESP_RST
- JP4 pad 2: E_COLCLK -> E_EN
- JP5 pad 1: P_PGEC -> P_LED1642_RST
- JP5 pad 2: E_COLSER -> D_LED1642_RST
- Q2 pad 3: P_ESP_RST -> E_EN
- Q29 pad 2: LEDLOGICVDD -> ESPVDD
- Q4 pad 3: P_ESP_GPIO0 -> E_GPIO0
- R1 pad 1: E_COLCLK -> P_MCLR
- R1 pad 2: Net-(R1-Pad2) -> /PIC_VDD
- R10 pad 1: ESPVDD -> SCL
- R10 pad 2: Net-(R10-Pad2) -> ESPVDD
- R11 pad 1: Net-(R11-Pad1) -> Net-(Q2-Pad1)
- R11 pad 2: /FILTVDD -> DTR
- R13 pad 1: P_ROW_DAT -> P_SER_DAT
- R13 pad 2: BUTTONSENSE -> P_BUTTON_SENSE
- R137 pad 2: P_ROW_DAT -> P_SPI_SDO
- R138 pad 2: P_ROW_CLK -> P_SER_CLK
- R139 pad 2: P_ROW_LAT -> P_SPI_SDI
- R14 pad 1: P_ESP_RST -> Net-(Q4-Pad1)
- R14 pad 2: Net-(R11-Pad1) -> RTS
- R140 pad 2: P_PWCLK_P -> P_SPI_CLK
- R141 pad 2: P_PWCLK_N -> P_PWCLK
- R146 pad 1: P_LED1642_RST -> D_LED1642_RST
- R15 pad 1: Net-(R15-Pad1) -> GND
- R15 pad 2: IR_IN -> D_LED1642_RST
- R16 pad 1: Net-(R16-Pad1) -> GND
- R16 pad 2: GND -> D_PWCLK_N
- R17 pad 1: Net-(R17-Pad1) -> GND
- R17 pad 2: HC595SER -> D_COLCLK
- R2 pad 1: E_COLLATCH -> Net-(R2-Pad1)
- R2 pad 2: Net-(R2-Pad2) -> P_SER_HC595_LAT
- R26 pad 1: Net-(R26-Pad1) -> GND
- R26 pad 2: E_AIN -> D_COLSER
- R27 pad 1: ESPVDD -> GND
- R27 pad 2: SDA -> D_COLLATCH
- R3 pad 1: E_COLSER -> Net-(R3-Pad1)
- R3 pad 2: Net-(R3-Pad2) -> P_RX
- R34 pad 1: Net-(R34-Pad1) -> GND
- R34 pad 2: GND -> D_ROW_LAT
- R4 pad 1: P_ESP_GPIO0 -> Net-(R4-Pad1)
- R4 pad 2: E_SDA -> P_TX
- R5 pad 2: /FILTVDD -> P_SER_DAT
- R6 pad 1: E_MCLR -> Net-(R6-Pad1)
- R6 pad 2: Net-(R34-Pad1) -> P_SER_LED1642_LAT
- R7 pad 1: Net-(D10-Pad2) -> P_SPI_SDO
- R7 pad 2: Net-(R10-Pad2) -> P_SER_RET
- R8 pad 1: ESPVDD -> P_SPI_SDO
- R8 pad 2: SCL -> GND
- R9 pad 1: ESPVDD -> SDA
- R9 pad 2: E_SDA -> ESPVDD
- SW3 pad 1: Net-(D1-Pad2) -> /row_driver/SWPAD_LEFT
- SW3 pad 2: BUTTONSENSE -> /row_driver/SWPAD_COM
- SW4 pad 1: Net-(D2-Pad2) -> /row_driver/SWPAD_UP
- SW4 pad 2: BUTTONSENSE -> /row_driver/SWPAD_COM
- SW5 pad 1: Net-(D3-Pad2) -> /row_driver/SWPAD_DOWN
- SW5 pad 2: BUTTONSENSE -> /row_driver/SWPAD_COM
- SW6 pad 1: Net-(D4-Pad2) -> /row_driver/SWPAD_RIGHT
- SW6 pad 2: BUTTONSENSE -> /row_driver/SWPAD_COM
- SW7 pad 1: Net-(D5-Pad2) -> /row_driver/SWPAD_OK
- SW7 pad 2: BUTTONSENSE -> /row_driver/SWPAD_COM
- SW8 pad 1: Net-(D6-Pad2) -> /row_driver/SWPAD_CANCEL
- SW8 pad 2: BUTTONSENSE -> /row_driver/SWPAD_COM
- U1 pad 1: /FILTVDD -> ESPVDD
- U1 pad 10: Net-(R15-Pad1) -> Net-(J1-Pad10)
- U1 pad 11: Net-(R127-Pad1) -> Net-(J1-Pad11)
- U1 pad 12: Net-(R126-Pad1) -> Net-(J1-Pad12)
- U1 pad 13: GND -> Net-(J1-Pad13)
- U1 pad 14: E_SCL -> GND
- U1 pad 15: Net-(R11-Pad1) -> Net-(J1-Pad15)
- U1 pad 16: Net-(R26-Pad1) -> Net-(J1-Pad16)
- U1 pad 17: Net-(R16-Pad1) -> Net-(J1-Pad17)
- U1 pad 18: GND -> Net-(J1-Pad18)
- U1 pad 2: Net-(R5-Pad1) -> E_EN
- U1 pad 3: Net-(R1-Pad2) -> Net-(J1-Pad3)
- U1 pad 4: Net-(R2-Pad2) -> Net-(J1-Pad4)
- U1 pad 5: Net-(R3-Pad2) -> Net-(J1-Pad5)
- U1 pad 6: Net-(R34-Pad1) -> Net-(J1-Pad6)
- U1 pad 7: Net-(R10-Pad2) -> Net-(J1-Pad7)
- U1 pad 8: E_SDA -> Net-(J1-Pad8)
- U1 pad 9: GND -> Net-(J1-Pad9)
- U14 pad 3: Net-(C1-Pad1) -> ESPVDD
- U15 pad 14: HC595SER -> COLSEROUT
- U19 pad 14: SCL -> Net-(R5-Pad1)
- U19 pad 15: SDA -> Net-(R6-Pad1)
- U19 pad 27: E_COLLATCH -> Net-(R2-Pad1)
- U19 pad 3: P_RX -> Net-(R3-Pad1)
- U19 pad 4: P_TX -> Net-(R4-Pad1)
- U2 pad 16: Net-(R17-Pad1) -> Net-(U2-Pad16)
- U2 pad 2: E_COLCLK -> D_COLCLK
- U2 pad 3: E_COLLATCH -> D_COLLATCH
- U2 pad 4: P_ROW_DAT -> GND
- U2 pad 5: P_PWCLK_N -> D_PWCLK_N
- U2 pad 6: P_PWCLK_P -> D_PWCLK_N
- U2 pad 7: P_ROW_CLK -> D_COLCLK
- U2 pad 8: P_ROW_LAT -> D_ROW_LAT
- U2 pad 9: E_COLSER -> D_COLSER
- W22 pad 1: HC595SER -> COLSEROUT
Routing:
- net /row_driver/SWPAD_COM: track 0.00 -> 112.9 mm, vias 0 -> 8
- net HC595SER: track 106.3 -> 0.00 mm, vias 2 -> 0
- net E_AIN: track 165.5 -> 70.9 mm, vias 2 -> 1
- net E_EN: track 0.00 -> 87.2 mm, vias 0 -> 6
- net COLSEROUT: track 230.1 -> 316.0 mm, vias 7 -> 4
- net P_SPI_SDO: track 0.00 -> 85.8 mm, vias 0 -> 1
- net E_TXD: track 85.5 -> 0.00 mm, vias 4 -> 0
- net GND: track 3084.8 -> 3166.2 mm, vias 88 -> 95
- net E_RXD: track 81.3 -> 0.00 mm, vias 3 -> 0
- net P_SPI_CLK: track 0.00 -> 80.6 mm, vias 0 -> 1
- net IR_IN: track 139.5 -> 60.7 mm
- net E_RX: track 0.00 -> 74.0 mm, vias 0 -> 4
- net /row_driver/SEL1: track 84.2 -> 157.6 mm, vias 3 -> 5
- net ESPVDD: track 254.5 -> 325.0 mm, vias 11 -> 10
- net RTS: track 83.8 -> 14.2 mm
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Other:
- board size 226 x 136 mm -> 246 x 136 mm
- board text added: "Ver 4.0 Proto 1"
- board text removed: "ANTENNA"
- board text removed: "BOOT"
- board text removed: "CANCEL"
- board text removed: "NC"
- board text removed: "OK"
- board text removed: "POWER"
- board text removed: "RST"
- board text removed: "STATUS"
- board text removed: "Ver 3.5 Proto 1"
- board text removed: "WROOM-02"

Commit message: Fixed button position; DRC clear
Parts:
- removed the REF** at (251.2, 63.4)
- removed the REF** at (249.3, 57.2)
- added REF**: stitch-via-0.6mm, components:stitch-via-0.6mm, F.Cu at (249.5, 67.4)
- added REF**: stitch-via-0.6mm, components:stitch-via-0.6mm, F.Cu at (249.7, 58.0)
- added REF**: stitch-via-0.6mm, components:stitch-via-0.6mm, F.Cu at (249.9, 60.1)
- added REF**: stitch-via-0.6mm, components:stitch-via-0.6mm, F.Cu at (250.1, 69.2)
- added REF**: stitch-via-0.6mm, components:stitch-via-0.6mm, F.Cu at (13.0, 131.3)
- added REF**: stitch-via-0.6mm, components:stitch-via-0.6mm, B.Cu at (13.1, 117.5)
- moved SW4 3.00 mm to (242.0, 59.0)
- moved REF** 0.86 mm to (31.4, 116.3)
- moved REF** 0.76 mm to (43.0, 116.4)
- moved REF** 0.71 mm to (26.9, 116.2)
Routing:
- net GND: track 3166.2 -> 3198.2 mm, vias 95 -> 96
- net /row_driver/SWPAD_RIGHT: track 50.1 -> 55.1 mm
- net /row_driver/SWPAD_UP: track 39.5 -> 34.9 mm
- net r4: track 402.5 -> 406.4 mm, vias 18 -> 20
- net /row_driver/SWPAD_COM: track 112.9 -> 110.6 mm
- net r6: track 417.4 -> 415.7 mm, vias 19 -> 18
- net /row_driver/SEL4: track 147.0 -> 147.7 mm
- net ce7: track 121.6 -> 121.1 mm
- net P_SPI_SDO: track 85.8 -> 85.3 mm
